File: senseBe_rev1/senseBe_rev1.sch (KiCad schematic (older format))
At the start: 34 parts, among them J1 PJ-32434_3-5mmAudioJack, P1 CONN_02X05, Q1 TSM2301, Q2 SI2302, Q3 SI2302, Q4 SI2302, SW1 SW_SPST, SW2 SW_DPST, U1 MDBT42Q, U2 TSSP4056, Y1 T38 Mercury

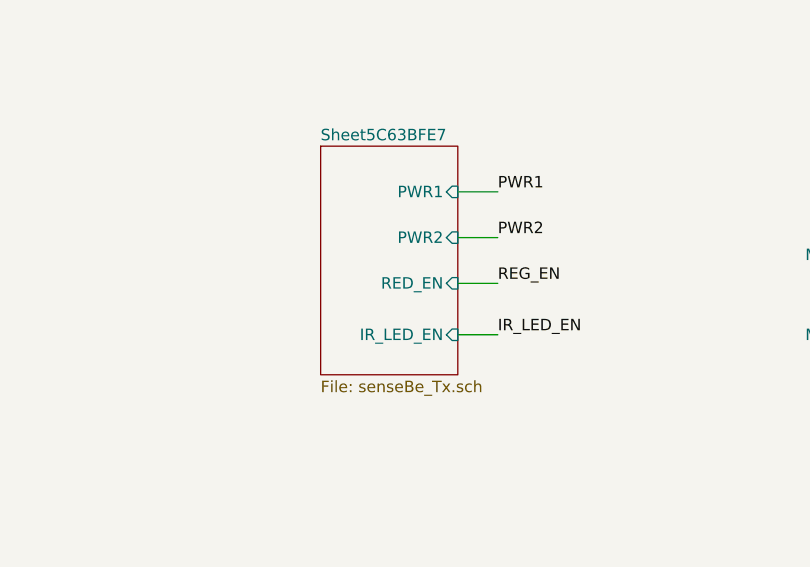
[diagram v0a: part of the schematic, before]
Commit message: Completes Schematic and PCB Design.
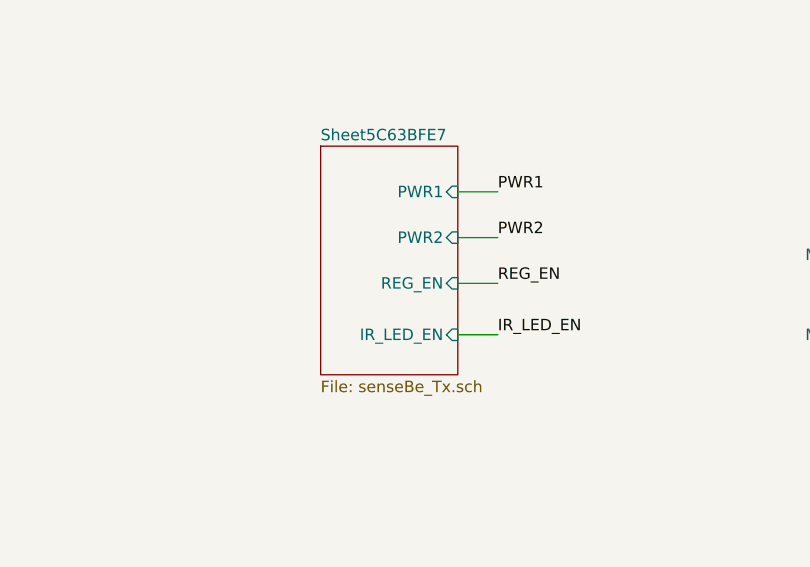
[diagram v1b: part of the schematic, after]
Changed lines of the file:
@@
 F2 "PWR1" I R 8875 5500 50
 F3 "PWR2" I R 8875 5700 50
-F4 "RED_EN" I R 8875 5900 50
+F4 "REG_EN" I R 8875 5900 50
 F5 "IR_LED_EN" I R 8875 6125 50
 $EndSheet

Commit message: Change dual LED pin connection, battery symbol now pinless
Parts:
- BT1: symbol Device:Battery_Cell -> senseBe_rev1:Device_Battery_Cell
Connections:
- net GND: now also SW1.1 (Pin_1); no longer BT1.2 (-)
- net at D2.2 (K1), R3.2: now also D3.4 (K2); no longer D3.2 (K1)
- net at D2.4 (K2), R4.2: now also D3.2 (K1); no longer D3.4 (K2)
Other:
- moved on the sheet: R3, R4
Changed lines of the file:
@@
 L senseBe_rev1-rescue:R-senseBeRx_rev1-senseBeRx_rev2-rescue-senseBeRx_rev3-rescue-senseBe_rev1-rescue R3
 U 1 1 5BA55B89
-P 5325 1500
-F 0 "R3" V 5225 1550 50  0000 L CNN
-F 1 "33" V 5325 1450 50  0000 L CNN
-F 2 "senseBe_rev1_fp:R_0603_HandSoldering" V 5255 1500 30  0001 C CNN
-F 3 "" H 5325 1500 30  0000 C CNN
-	1    5325 1500
+P 5450 1500
+F 0 "R3" V 5350 1550 50  0000 L CNN
+F 1 "33" V 5450 1450 50  0000 L CNN
+F 2 "senseBe_rev1_fp:R_0603_HandSoldering" V 5380 1500 30  0001 C CNN
+F 3 "" H 5450 1500 30  0000 C CNN
+	1    5450 1500
 	0    1    1    0
 $EndComp
@@
 L senseBe_rev1-rescue:R-senseBeRx_rev1-senseBeRx_rev2-rescue-senseBeRx_rev3-rescue-senseBe_rev1-rescue R4
 U 1 1 5BA55CAF
-P 5325 1700
-F 0 "R4" V 5425 1725 50  0000 L CNN
-F 1 "24" V 5325 1650 50  0000 L CNN
-F 2 "senseBe_rev1_fp:R_0603_HandSoldering" V 5255 1700 30  0001 C CNN
-F 3 "" H 5325 1700 30  0000 C CNN
-	1    5325 1700
+P 5450 1700
+F 0 "R4" V 5550 1725 50  0000 L CNN
+F 1 "24" V 5450 1650 50  0000 L CNN
+F 2 "senseBe_rev1_fp:R_0603_HandSoldering" V 5380 1700 30  0001 C CNN
+F 3 "" H 5450 1700 30  0000 C CNN
+	1    5450 1700
 	0    1    1    0
 $EndComp
 Wire Wire Line
-	5075 1500 5150 1500
-Wire Wire Line
-	5075 1700 5100 1700
-Wire Wire Line
-	5475 1500 6100 1500
-Wire Wire Line
-	5475 1700 5875 1700
+	5600 1500 6100 1500
+Wire Wire Line
+	5600 1700 5875 1700
 Wire Wire Line
 	5875 1700 5875 1850
@@
 LIGHT_SENSE
 $Comp
-L Device:Battery_Cell BT1
+L senseBe_rev1:Device_Battery_Cell BT1
 U 1 1 5A868475
 P 1050 1325
@@
 	2500 1675 2500 1425
 Wire Wire Line
-	1050 1425 1050 1675
-Wire Wire Line
 	1850 1275 1850 1675
 Connection ~ 1850 1675
@@
 Wire Wire Line
 	1050 1675 1850 1675
-Wire Wire Line
-	1050 975  1050 1125
 $Comp
 L Connector_Generic:Conn_01x02 SW2
@@
 	5075 1050 5100 1050
 Wire Wire Line
-	5100 1050 5100 1700
-Connection ~ 5100 1700
-Wire Wire Line
-	5100 1700 5175 1700
-Wire Wire Line
 	5075 850  5150 850
-Wire Wire Line
-	5150 850  5150 1500
-Connection ~ 5150 1500
-Wire Wire Line
-	5150 1500 5175 1500
 Wire Wire Line
 	9050 5500 8875 5500
@@
 Wire Wire Line
 	3750 3975 4500 3975
+Wire Wire Line
+	5075 1700 5150 1700
+Wire Wire Line
+	5075 1500 5100 1500
+Wire Wire Line
+	5150 850  5150 1700
+Connection ~ 5150 1700
+Wire Wire Line
+	5150 1700 5300 1700
+Wire Wire Line
+	5100 1050 5100 1500
+Connection ~ 5100 1500
+Wire Wire Line
+	5100 1500 5300 1500
+Wire Wire Line
+	1050 975  1050 1675
 $EndSCHEMATC
